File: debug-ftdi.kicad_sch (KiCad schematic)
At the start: 84 parts, among them J13 U_FL-R-SMT-1, J14 U_FL-R-SMT-1, J15 U_FL-R-SMT-1, J16 U_FL-R-SMT-1, J3 USB-C_GCT_USB4105-GF-A, J9 U_FL-R-SMT-1, Q20 BSS84AKW, U13 TXU0304BQAR, U16 TXS0102DQER, U32 TXS0102DQER, U5 NCP718BSN330T1G, U6 FT4232H_VQFN, U7 TXU0304BQAR, U8 TPD4E05U06QDQARQ1, U9 SN74HC595B, Y1 Resonator_12MHz_ABM8G

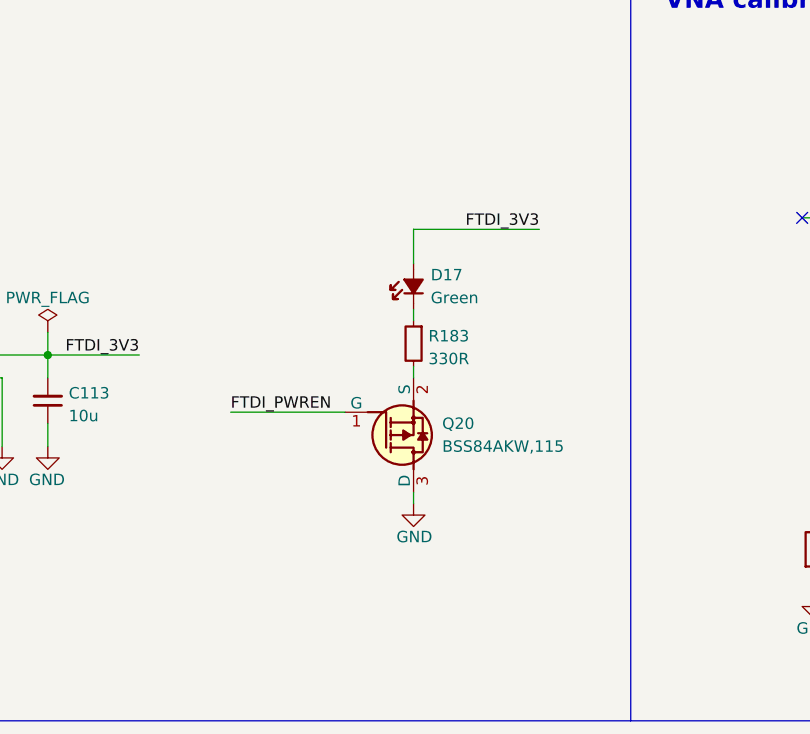
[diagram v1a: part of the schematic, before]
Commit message: [#69518] Fix Q20 configuration
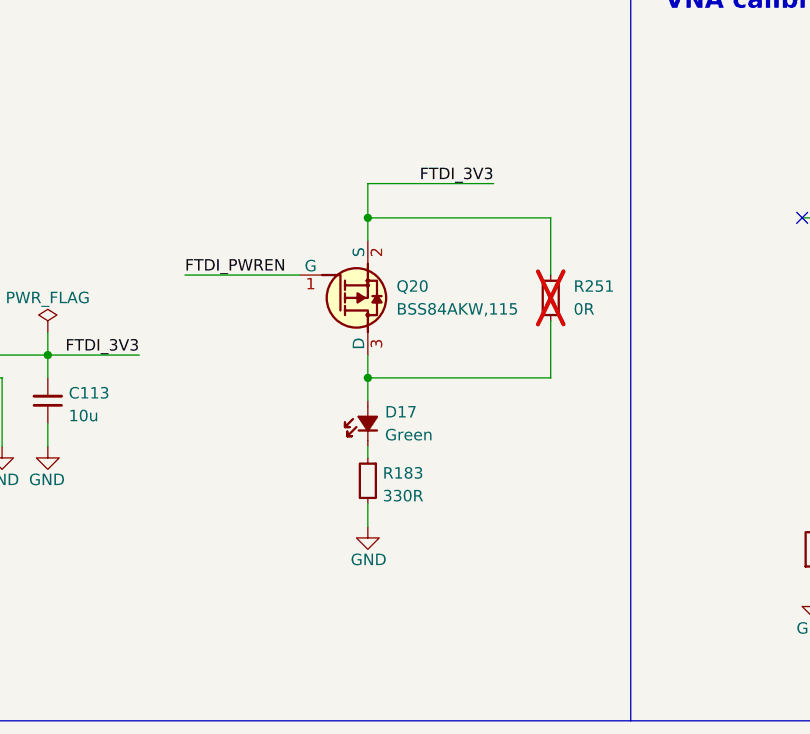
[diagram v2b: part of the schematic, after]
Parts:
- added R251: R_0R_0402, antmicro-footprints:R_0402_1005Metric, symbol antmicroResistors0402:R_0R_0402
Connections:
- net FTDI_3V3: now also Q20.2 (S), R251.2; no longer D17.2 (A)
- net GND: now also R183.2; no longer Q20.3 (D)
- new net: D17.2 (A), Q20.3 (D), R251.1
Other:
- moved on the sheet: D17, Q20, R183

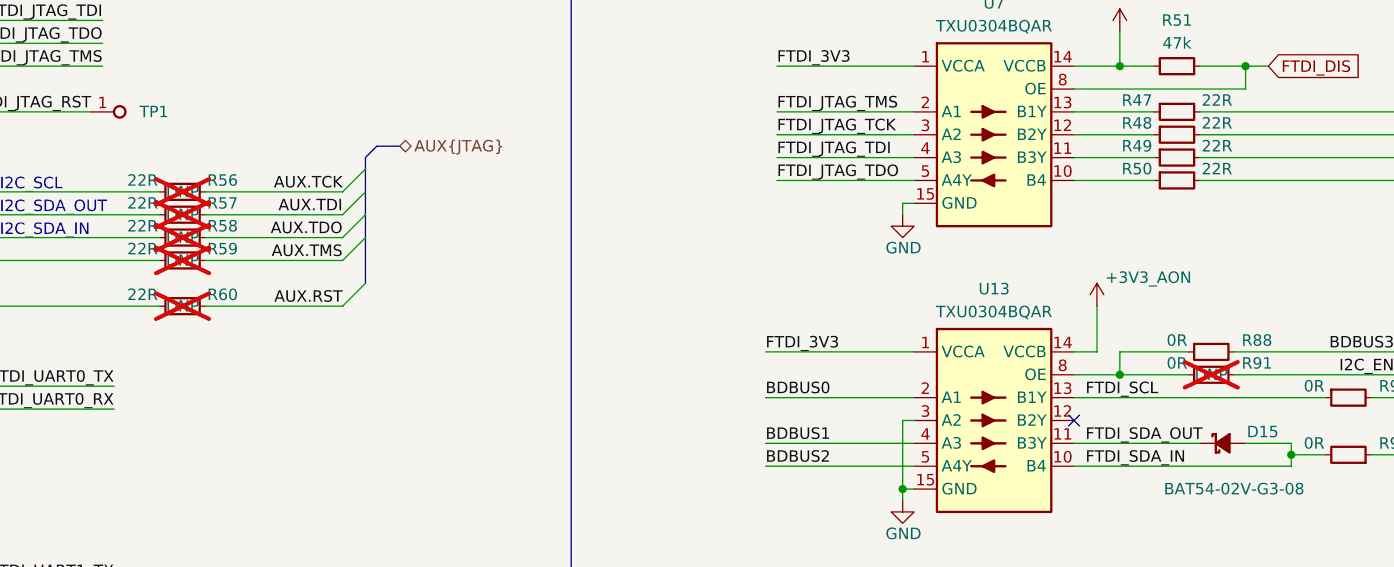
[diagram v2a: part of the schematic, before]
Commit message: [#69629] Fix DNP attributes
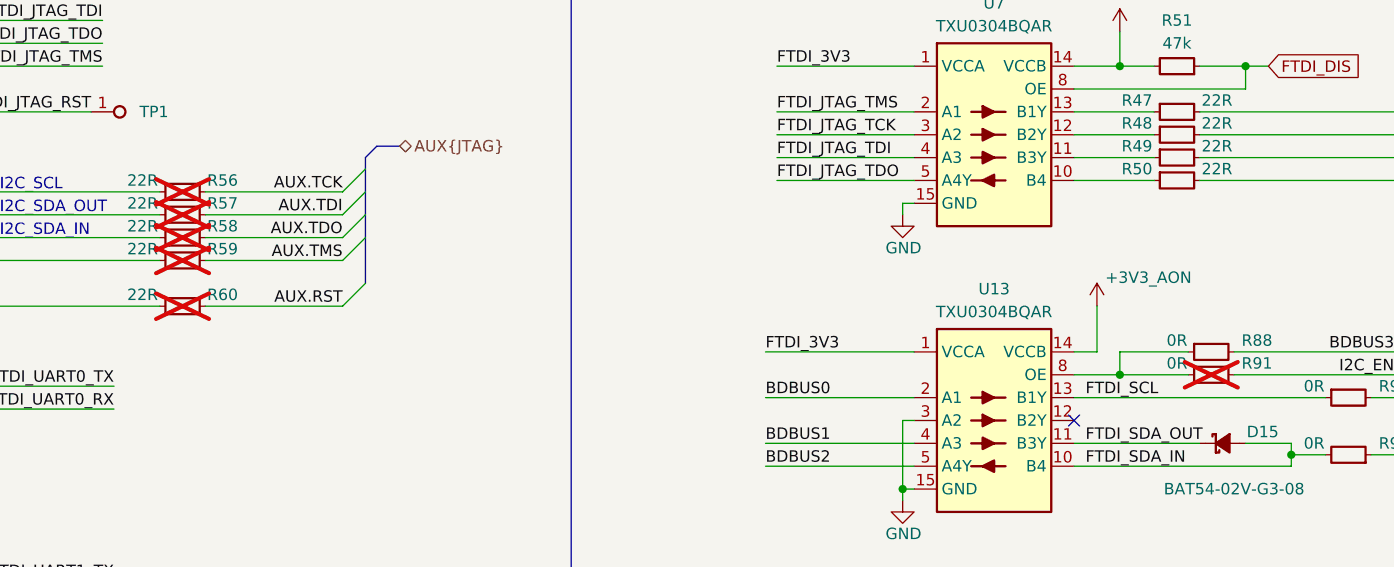
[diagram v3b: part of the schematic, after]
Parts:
- R251: now left out of the parts list
- R56, R57, R58, R59, R60, R91: DNP DNP -> (none)
